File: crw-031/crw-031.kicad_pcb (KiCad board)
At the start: 4 copper layers, 18.3 x 47 mm, 38 parts, among them J1 PICKIT, J2 L, J3 R, J4 USB_C_Receptacle_USB2.0_16P, SW1 BOOT, SW2 RESET, U1 PIC32MX250F128D-IPT, U2 USBLC6-2SC6, U3 MCP1703Ax-500xxDB, U4 MCP1703Ax-330xxTT, Y1 8MHz

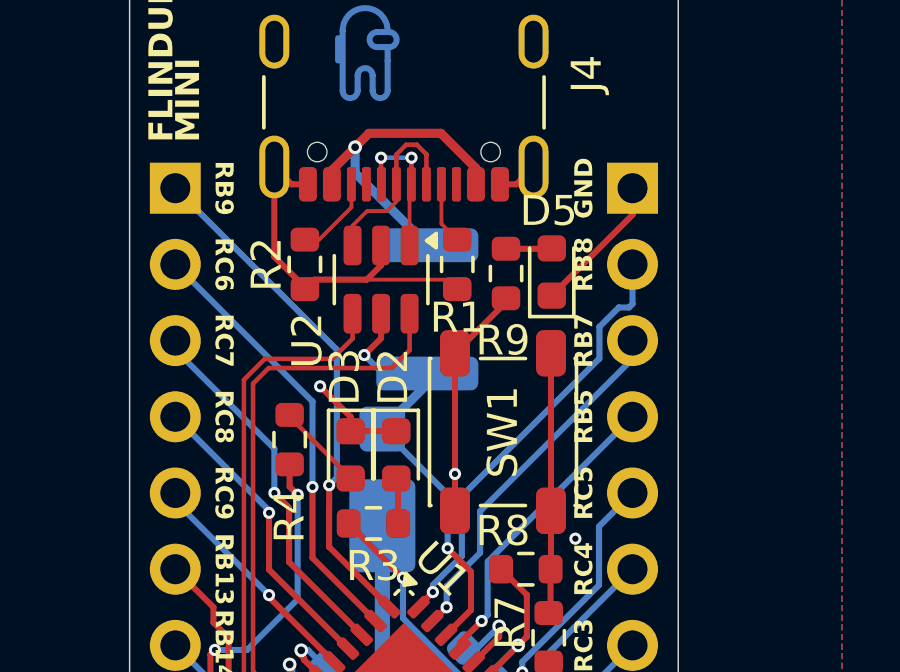
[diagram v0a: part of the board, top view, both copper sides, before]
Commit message: Tweak FMini
- FIx LED footprints
- move stuff around in schematic
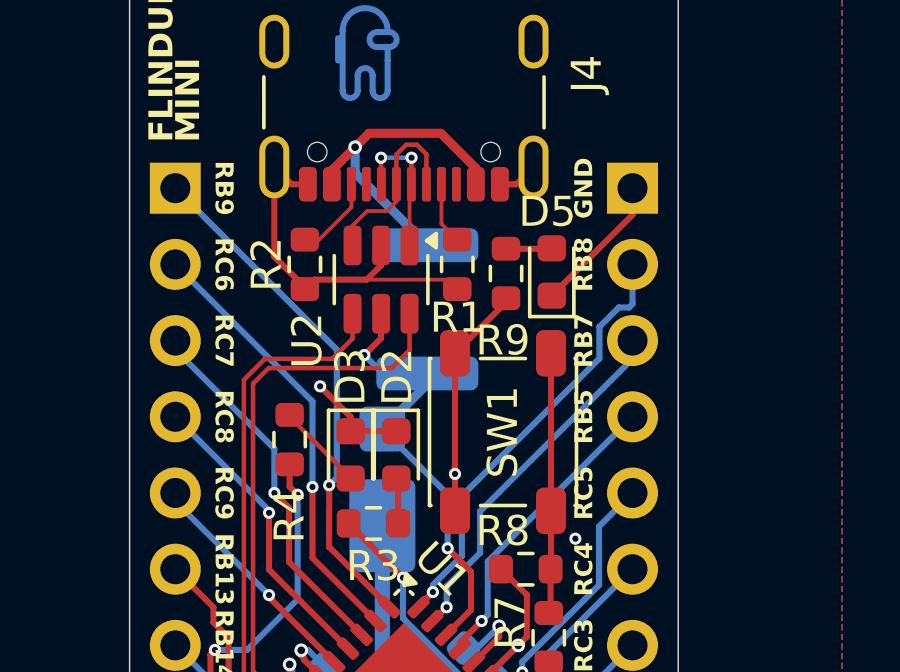
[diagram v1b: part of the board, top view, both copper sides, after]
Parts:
- D2, D3, D5: footprint Diode_SMD:D_0603_1608Metric -> LED_SMD:LED_0603_1608Metric
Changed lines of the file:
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@@
 		)
 	)
-	(footprint "Diode_SMD:D_0603_1608Metric"
+	(footprint "LED_SMD:LED_0603_1608Metric"
 		(layer "F.Cu")
 		(at 75.692 69.85 -90)
-		(descr "Diode SMD 0603 (1608 Metric), square (rectangular) end terminal, IPC_7351 nominal, (Body size source: http://www.tortai-tech.com/upload/download/2011102023233369053.pdf), generated with kicad-footprint-generator")
-		(tags "diode")
+		(descr "LED SMD 0603 (1608 Metric), square (rectangular) end terminal, IPC_7351 nominal, (Body size source: http://www.tortai-tech.com/upload/download/2011102023233369053.pdf), generated with kicad-footprint-generator")
+		(tags "LED")
 		(property "Reference" "D3"
-			(at -2.6 0.192 90)
+			(at -2.6 0 -90)
 			(layer "F.SilkS")
 			(effects
@@
 		)
 		(property "Value" "LED1"
-			(at 0 1.43 90)
+			(at 0 1.43 -90)
 			(layer "F.Fab")
 			(effects
@@
 			)
 		)
-		(property "Footprint" "Diode_SMD:D_0603_1608Metric"
+		(property "Footprint" "LED_SMD:LED_0603_1608Metric"
 			(at 0 0 -90)
 			(unlocked yes)
@@
 		)
 		(fp_text user "${REFERENCE}"
-			(at 0 0 90)
+			(at 0 0 -90)
 			(layer "F.Fab")
 			(effects
@@
 		)
 		(pad "1" smd roundrect
-			(at -0.787501 0 270)
+			(at -0.7875 0 270)
 			(size 0.875 0.95)
 			(layers "F.Cu" "F.Paste" "F.Mask")
@@
 		)
 		(pad "2" smd roundrect
-			(at 0.787501 0 270)
+			(at 0.7875 0 270)
 			(size 0.875 0.95)
 			(layers "F.Cu" "F.Paste" "F.Mask")
@@
 			(pintype "passive")
 		)
-		(model "${KICAD8_3DMODEL_DIR}/Diode_SMD.3dshapes/D_0603_1608Metric.wrl"
+		(model "${KICAD8_3DMODEL_DIR}/LED_SMD.3dshapes/LED_0603_1608Metric.wrl"
 			(offset
 				(xyz 0 0 0)
@@
 		)
 	)
-	(footprint "Diode_SMD:D_0603_1608Metric"
+	(footprint "LED_SMD:LED_0603_1608Metric"
 		(layer "F.Cu")
 		(at 77.216 69.85 -90)
-		(descr "Diode SMD 0603 (1608 Metric), square (rectangular) end terminal, IPC_7351 nominal, (Body size source: http://www.tortai-tech.com/upload/download/2011102023233369053.pdf), generated with kicad-footprint-generator")
-		(tags "diode")
+		(descr "LED SMD 0603 (1608 Metric), square (rectangular) end terminal, IPC_7351 nominal, (Body size source: http://www.tortai-tech.com/upload/download/2011102023233369053.pdf), generated with kicad-footprint-generator")
+		(tags "LED")
 		(property "Reference" "D2"
-			(at -2.6 0.1016 -90)
+			(at -2.6 -0.034 -90)
 			(layer "F.SilkS")
 			(effects
@@
 		)
 		(property "Value" "LED2"
-			(at 0 1.43 90)
+			(at 0 1.43 -90)
 			(layer "F.Fab")
 			(effects
@@
 			)
 		)
-		(property "Footprint" "Diode_SMD:D_0603_1608Metric"
+		(property "Footprint" "LED_SMD:LED_0603_1608Metric"
 			(at 0 0 -90)
 			(unlocked yes)
@@
 		)
 		(fp_text user "${REFERENCE}"
-			(at 0 0 90)
+			(at 0 0 -90)
 			(layer "F.Fab")
 			(effects
@@
 		)
 		(pad "1" smd roundrect
-			(at -0.787501 0 270)
+			(at -0.7875 0 270)
 			(size 0.875 0.95)
 			(layers "F.Cu" "F.Paste" "F.Mask")
@@
 		)
 		(pad "2" smd roundrect
-			(at 0.787501 0 270)
+			(at 0.7875 0 270)
 			(size 0.875 0.95)
 			(layers "F.Cu" "F.Paste" "F.Mask")
@@
 			(pintype "passive")
 		)
-		(model "${KICAD8_3DMODEL_DIR}/Diode_SMD.3dshapes/D_0603_1608Metric.wrl"
+		(model "${KICAD8_3DMODEL_DIR}/LED_SMD.3dshapes/LED_0603_1608Metric.wrl"
 			(offset
 				(xyz 0 0 0)
@@
 		)
 	)
-	(footprint "Diode_SMD:D_0603_1608Metric"
+	(footprint "LED_SMD:LED_0603_1608Metric"
 		(layer "F.Cu")
 		(at 82.3976 63.754 90)
-		(descr "Diode SMD 0603 (1608 Metric), square (rectangular) end terminal, IPC_7351 nominal, (Body size source: http://www.tortai-tech.com/upload/download/2011102023233369053.pdf), generated with kicad-footprint-generator")
-		(tags "diode")
+		(descr "LED SMD 0603 (1608 Metric), square (rectangular) end terminal, IPC_7351 nominal, (Body size source: http://www.tortai-tech.com/upload/download/2011102023233369053.pdf), generated with kicad-footprint-generator")
+		(tags "LED")
 		(property "Reference" "D5"
-			(at 2.032 -0.1016 180)
+			(at 2.004 -0.1476 180)
 			(layer "F.SilkS")
 			(effects
@@
 			)
 		)
-		(property "Footprint" "Diode_SMD:D_0603_1608Metric"
+		(property "Footprint" "LED_SMD:LED_0603_1608Metric"
 			(at 0 0 90)
 			(unlocked yes)
@@
 		)
 		(pad "1" smd roundrect
-			(at -0.787501 0 90)
+			(at -0.7875 0 90)
 			(size 0.875 0.95)
 			(layers "F.Cu" "F.Paste" "F.Mask")
@@
 		)
 		(pad "2" smd roundrect
-			(at 0.787501 0 90)
+			(at 0.7875 0 90)
 			(size 0.875 0.95)
 			(layers "F.Cu" "F.Paste" "F.Mask")
@@
 			(pintype "passive")
 		)
-		(model "${KICAD8_3DMODEL_DIR}/Diode_SMD.3dshapes/D_0603_1608Metric.wrl"
+		(model "${KICAD8_3DMODEL_DIR}/LED_SMD.3dshapes/LED_0603_1608Metric.wrl"
 			(offset
 				(xyz 0 0 0)
